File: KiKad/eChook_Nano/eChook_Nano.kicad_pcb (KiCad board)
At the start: 2 copper layers, 75 x 75 mm, 112 parts, among them J1 Expansion, Q2 Q_NMOS-D_Generic_GSD, Q3 Q_NMOS-D_Generic_GSD, U1 Arduino_Nano_v3.x, U2 TSR_1-2450, U3 MCP6002-xP

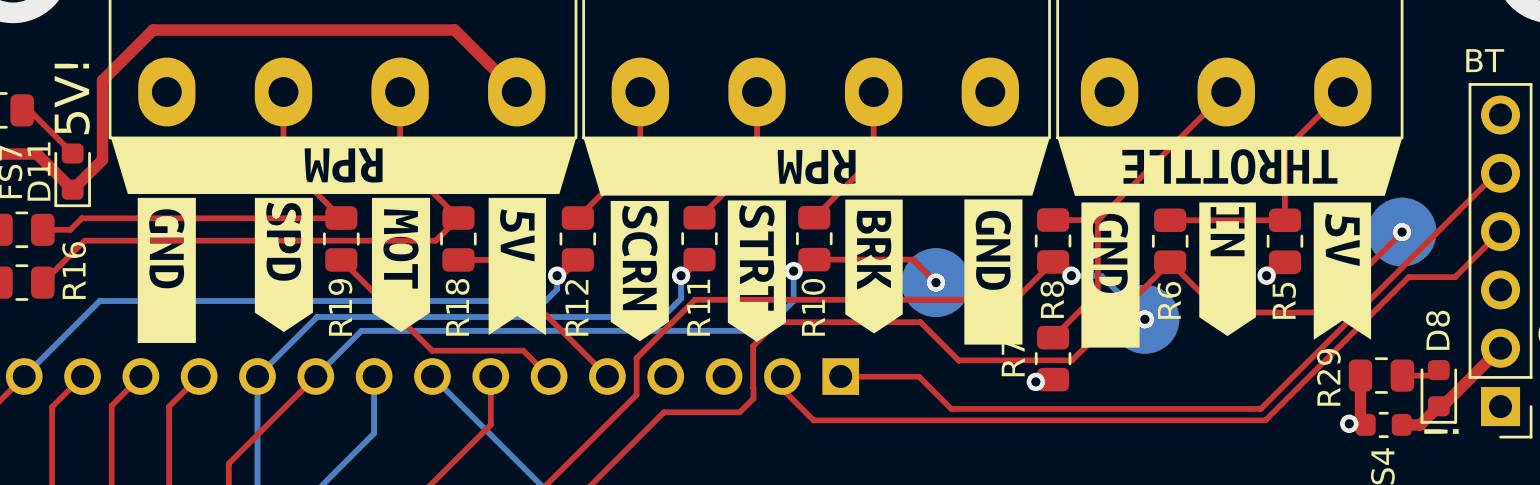
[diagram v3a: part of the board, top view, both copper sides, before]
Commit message: connector Labels corrected
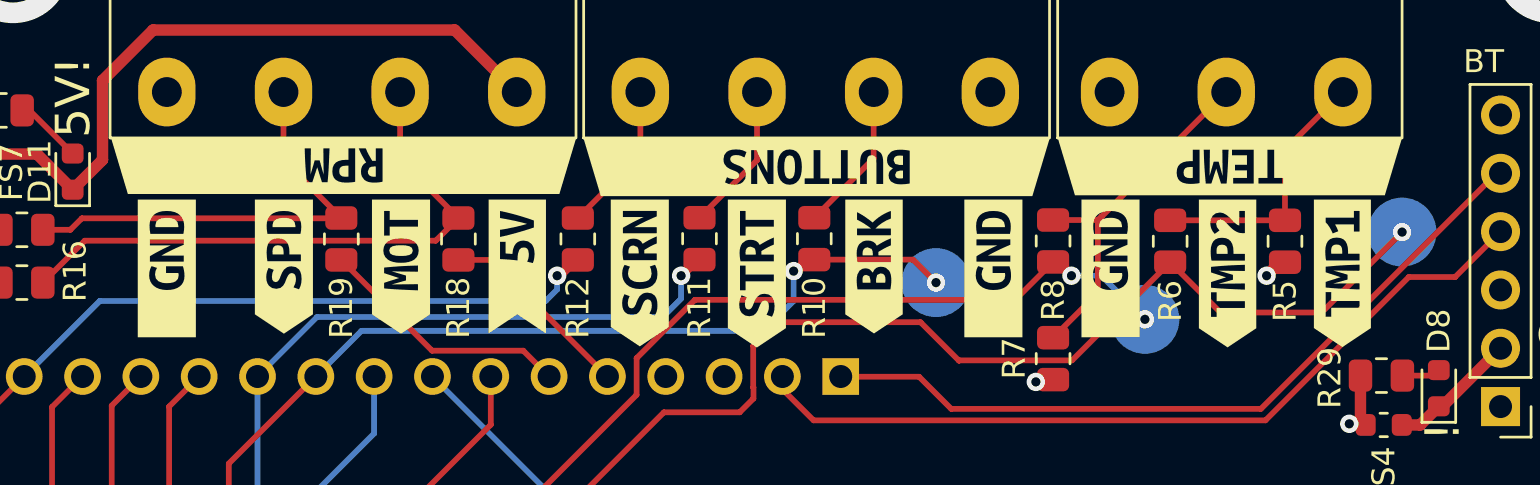
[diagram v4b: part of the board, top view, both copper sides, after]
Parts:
- removed the kibuzzard-66D72019 at (156.2, 79.0)
- removed the kibuzzard-66D72019 at (120.2, 79.0)
- removed the kibuzzard-66D72019 at (161.3, 79.2)
- removed the kibuzzard-66D72613 at (171.4, 79.0)
- removed the kibuzzard-66D72613 at (135.5, 78.8)
- removed the kibuzzard-66D728C6 at (166.4, 78.9)
- removed the kibuzzard-66D728F7 at (166.5, 74.5)
- removed the kibuzzard-66D72A35 at (148.5, 74.5)
- removed kibuzzard-66D72A68: G***, kibuzzard-66D72A68
- removed kibuzzard-66D72A7D: G***, kibuzzard-66D72A7D
- removed kibuzzard-66D72AFE: G***, kibuzzard-66D72AFE
- removed kibuzzard-66D72B0C: G***, kibuzzard-66D72B0C
- removed kibuzzard-66D72B26: G***, kibuzzard-66D72B26
- added kibuzzard-66D86D8A: G***, kibuzzard-66D86D8A, F.Cu at (148.5, 74.5)
- added kibuzzard-66D86D91: G***, kibuzzard-66D86D91, F.Cu at (166.5, 74.5)
- added kibuzzard-66D86E8F: G***, kibuzzard-66D86E8F, F.Cu at (125.3, 78.8)
- added kibuzzard-66D86EA3: G***, kibuzzard-66D86EA3, F.Cu at (130.4, 78.8)
- added kibuzzard-66D86EBA: G***, kibuzzard-66D86EBA, F.Cu at (135.5, 78.8)
- added kibuzzard-66D86EDC: G***, kibuzzard-66D86EDC, F.Cu at (140.8, 79.1)
- added kibuzzard-66D86F00: G***, kibuzzard-66D86F00, F.Cu at (145.9, 79.1)
- added kibuzzard-66D86F2B: G***, kibuzzard-66D86F2B, F.Cu at (151.0, 78.8)
- added kibuzzard-66D86F40: G***, kibuzzard-66D86F40, F.Cu at (120.2, 78.9)
- added kibuzzard-66D86F46: G***, kibuzzard-66D86F46, F.Cu at (156.2, 78.9)
- added kibuzzard-66D86F51: G***, kibuzzard-66D86F51, F.Cu at (161.3, 78.9)
- added kibuzzard-66D86F60: G***, kibuzzard-66D86F60, F.Cu at (166.4, 79.1)
- added kibuzzard-66D86F7C: G***, kibuzzard-66D86F7C, F.Cu at (171.4, 79.1)

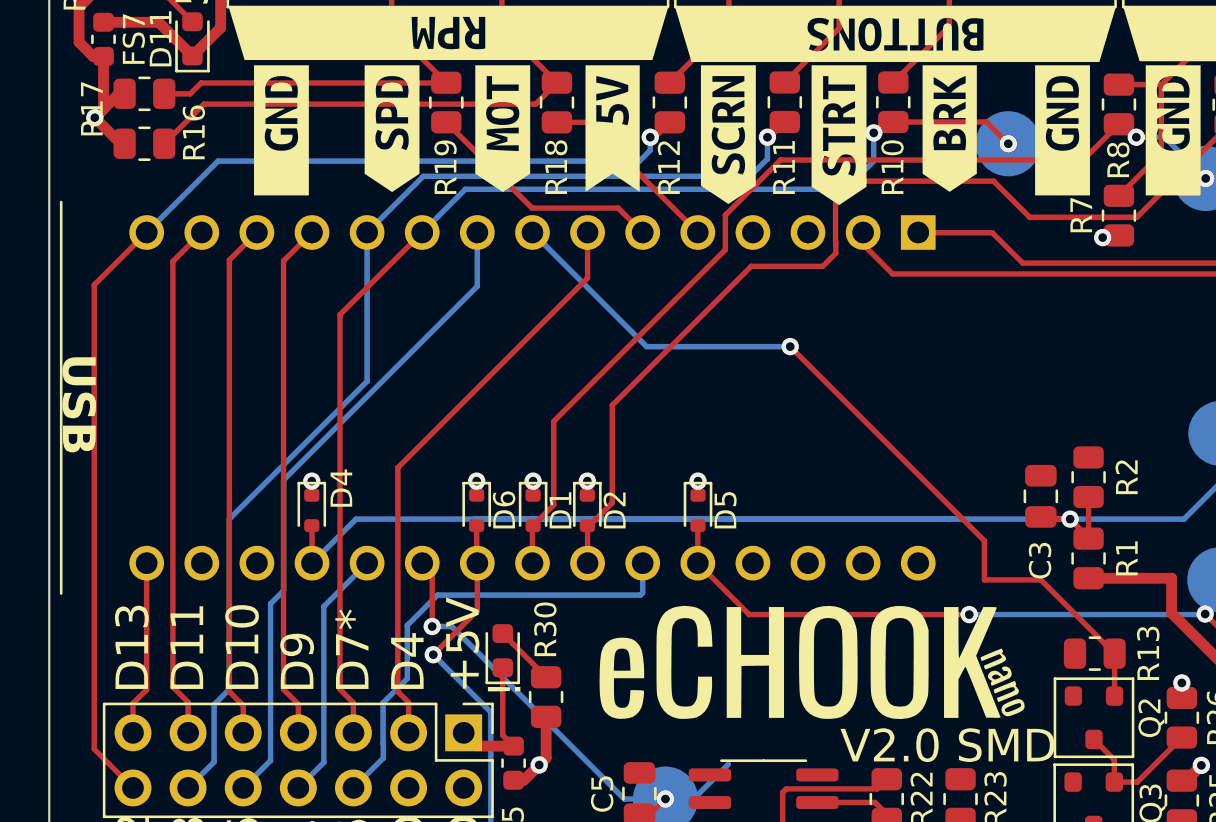
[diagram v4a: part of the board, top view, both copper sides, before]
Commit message: Added ground plane under nano
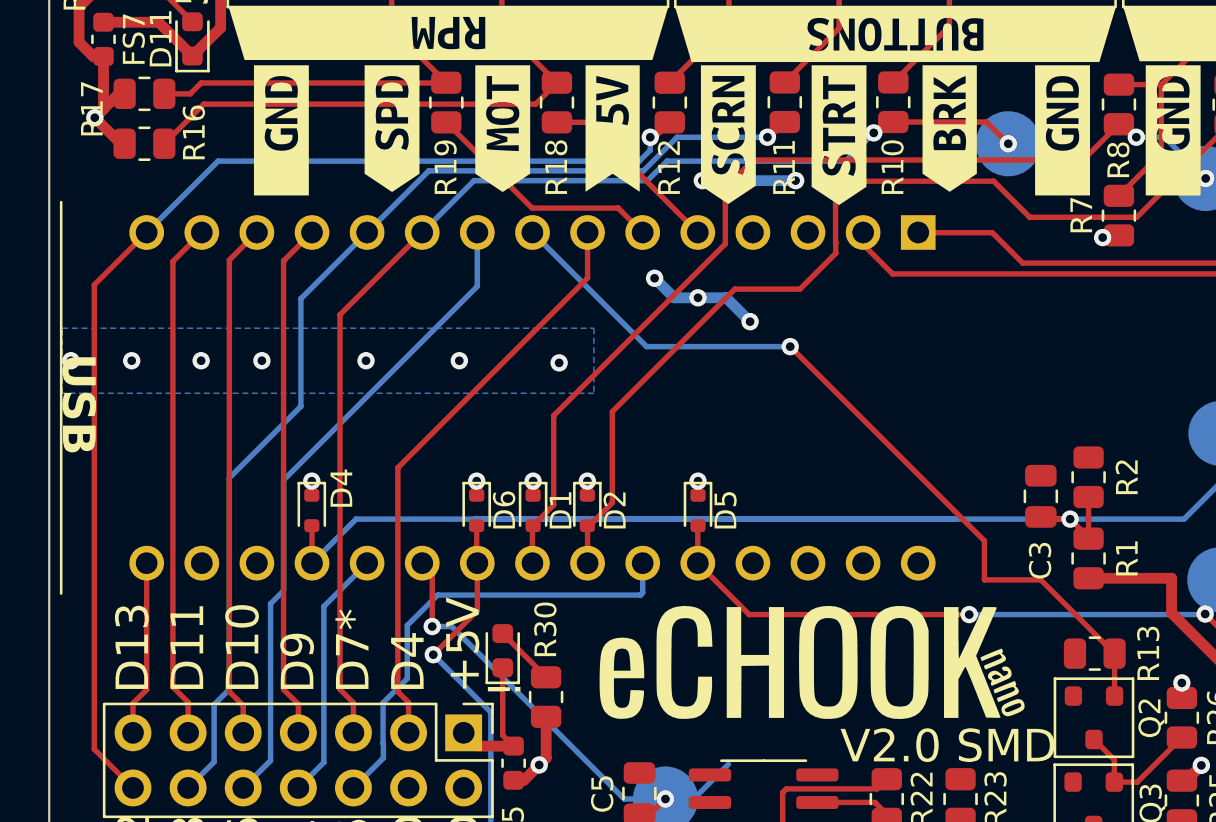
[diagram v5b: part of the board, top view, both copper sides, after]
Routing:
- net GND: track 0.00 -> 9.71 mm, vias 1 -> 13
- net /Brake: track 55.2 -> 54.4 mm
- net /Temp2: track 43.6 -> 44.3 mm
- net /DriverButton: track 51.0 -> 50.4 mm
- added copper zone on B.Cu, net GND
